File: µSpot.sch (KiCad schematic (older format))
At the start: 35 parts, among them J1 Conn_01x03, SW1 Rotary_Encoder_Switch, U1 AP65211A, U2 MIC5365-3.3YD5, U3 ATtiny406-S, U4 OLED_Display_9616

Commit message: Layout finish
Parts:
- removed C10, C11, C7, C8: 1u, Capacitor_SMD:C_1206_3216Metric_Pad1.42x1.75mm_HandSolder, symbol Device:C_Small
- removed R10: 390k, Resistor_SMD:R_1206_3216Metric_Pad1.42x1.75mm_HandSolder, symbol Device:R_Small
- removed U1: AP65211A, Package_TO_SOT_SMD:TSOT-23-6_HandSoldering, symbol microSpot:AP65211A
- removed U3: ATtiny406-S, Package_SO:SOIC-20W_7.5x12.8mm_P1.27mm, symbol MCU_Microchip_ATtiny:ATtiny406-S
- removed U4: OLED_Display_9616, µSpot:OLED_Display_9616, symbol microSpot:OLED_Display_9616
- added D1: Red, LED_SMD:LED_0805_2012Metric_Pad1.15x1.40mm_HandSolder, symbol Device:LED
- added D2: 2SS100L-W, Diode_SMD:D_SOD-123F, symbol Device:D_Schottky_Small
- added J2: Conn_01x04, Connector_PinSocket_2.54mm:PinSocket_1x04_P2.54mm_Vertical_SMD_Pin1Left, symbol Connector_Generic:Conn_01x04
- added Q7: Q_PMOS_DGS, Package_TO_SOT_SMD:SOT-23, symbol Device:Q_PMOS_DGS
- added R10: 10k, Resistor_SMD:R_0805_2012Metric_Pad1.15x1.40mm_HandSolder, symbol Device:R
- added U1: AP65111AWU, Package_TO_SOT_SMD:TSOT-23-6, symbol Regulator_Switching:AP65111AWU
- added U3: ATtiny404-SS, Package_SO:SOIC-14_3.9x8.7mm_P1.27mm, symbol MCU_Microchip_ATtiny:ATtiny404-SS
- added U5: ADS7029, Package_SO:VSSOP-8_2.3x2mm_P0.5mm, symbol Analog_ADC:ADS7029
- C1, C5: footprint Capacitor_SMD:C_1206_3216Metric_Pad1.42x1.75mm_HandSolder -> Capacitor_SMD:C_0805_2012Metric_Pad1.18x1.45mm_HandSolder
- C2, C3, C4, C6: footprint Capacitor_SMD:C_1206_3216Metric_Pad1.42x1.75mm_HandSolder -> Capacitor_SMD:C_0805_2012Metric_Pad1.15x1.40mm_HandSolder
- C9: value 1u -> 3.3u; footprint Capacitor_SMD:C_1206_3216Metric_Pad1.42x1.75mm_HandSolder -> Capacitor_SMD:C_0805_2012Metric_Pad1.15x1.40mm_HandSolder
- D3, D4: footprint LED_SMD:LED_1206_3216Metric_Pad1.42x1.75mm_HandSolder -> LED_SMD:LED_0805_2012Metric_Pad1.15x1.40mm_HandSolder
- L1: footprint Inductor_SMD:L_Taiyo-Yuden_MD-2020 -> Inductor_SMD:L_0805_2012Metric_Pad1.15x1.40mm_HandSolder
- R1, R3: value 4k7 -> 10k; footprint Resistor_SMD:R_1206_3216Metric_Pad1.42x1.75mm_HandSolder -> Resistor_SMD:R_0805_2012Metric_Pad1.15x1.40mm_HandSolder
- R11: value 10k -> 100k; footprint Resistor_SMD:R_1206_3216Metric_Pad1.42x1.75mm_HandSolder -> Resistor_SMD:R_0805_2012Metric_Pad1.20x1.40mm_HandSolder
- R2, R4, R5, R6, R7, R8, R9: footprint Resistor_SMD:R_1206_3216Metric_Pad1.42x1.75mm_HandSolder -> Resistor_SMD:R_0805_2012Metric_Pad1.15x1.40mm_HandSolder
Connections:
- net ON_LED is gone; now on net TRIGGER: R1.1
- net +3V3: now also C9.1, J2.2 (Pin_2), U3.1 (VCC), U5.7 (AVDD); no longer R11.1
- net +5V: now also D2.1 (K), Q7.3 (S); no longer C5.1, J1.3 (Pin_3), L1.2, R4.1
- net +BATT: now also U1.1 (IN)
- net BAT_VOL: now also U3.2 (PA4)
- net CLK: now also U3.6 (PB3)
- net DT: now also U3.7 (PB2)
- net GND: now also C9.2, J1.1 (Pin_1), R11.2, D1.1 (K), J2.1 (Pin_1), U1.2 (GND), U3.14 (GND), U5.8 (GND); no longer J1.2 (Pin_2)
- net SCL: now also R8.2, J2.3 (Pin_3), U3.9 (PB0); no longer R9.2
- net SDA: now also R9.2, J2.4 (Pin_4), U3.8 (PB1); no longer R8.2
- net SWITCH: now also U3.5 (PA7)
- net TEMP: now also U3.3 (PA5)
- net TRIGGER: now also U3.4 (PA6)
- net UDPI: now also J1.2 (Pin_2), U3.10 (~RESET~/PA0); no longer J1.1 (Pin_1)
- net at C4.2, L1.1: now also U1.3 (SW)
- net at R2.2: now also U1.6 (FB)
- net at C4.1: now also U1.4 (BST)
- new net: D1.2 (A), R10.2
- new net +5VA: C5.1, L1.2, Q7.1 (D), R10.1, R4.1
- new net +5VP: D2.2 (A), J1.3 (Pin_3), Q7.2 (G), R11.1
- new net SCLK: U3.13 (PA3), U5.2 (SCLK)
- new net WELD+: U5.6 (AINP)
- new net WELD-: U5.5 (AINM)
- new net WELD_ADC: U3.12 (PA2), U5.3 (SDO)
- new net WELD_CS: U3.11 (PA1), U5.4 (~CS)
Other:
- note added: "ADC\n"
- moved on the sheet: C1, C4, C5, C6, L1, R2, R4, R5, R8, R9

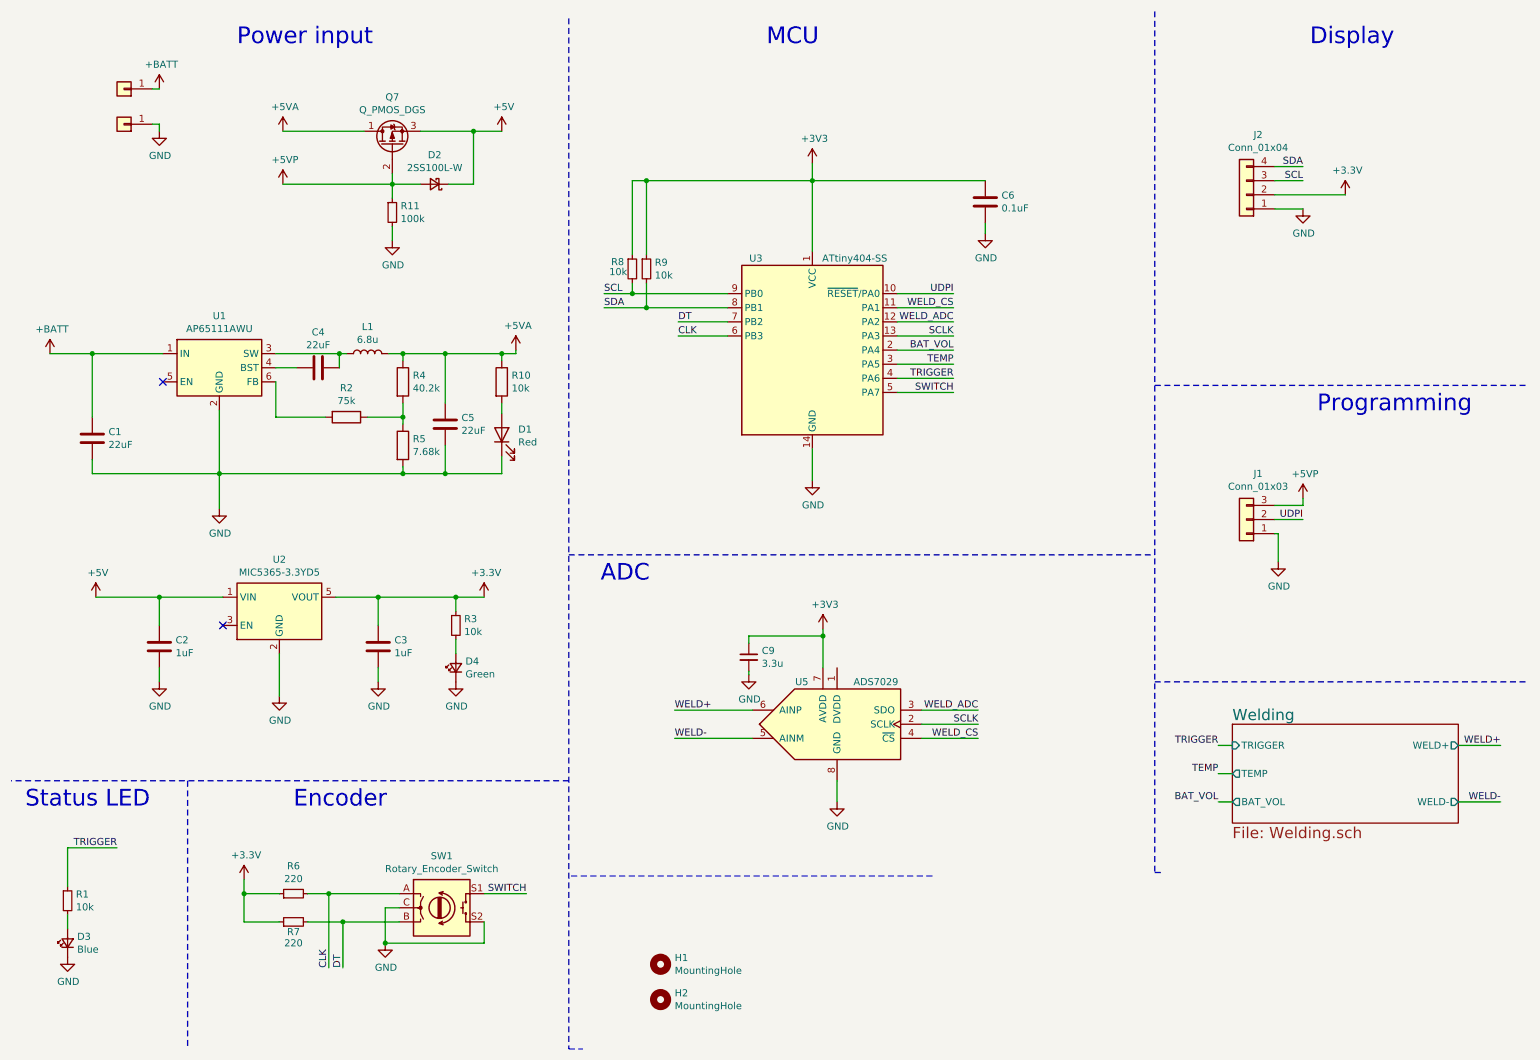
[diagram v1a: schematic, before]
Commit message: Changes FAN3111 footprint and removed 5V
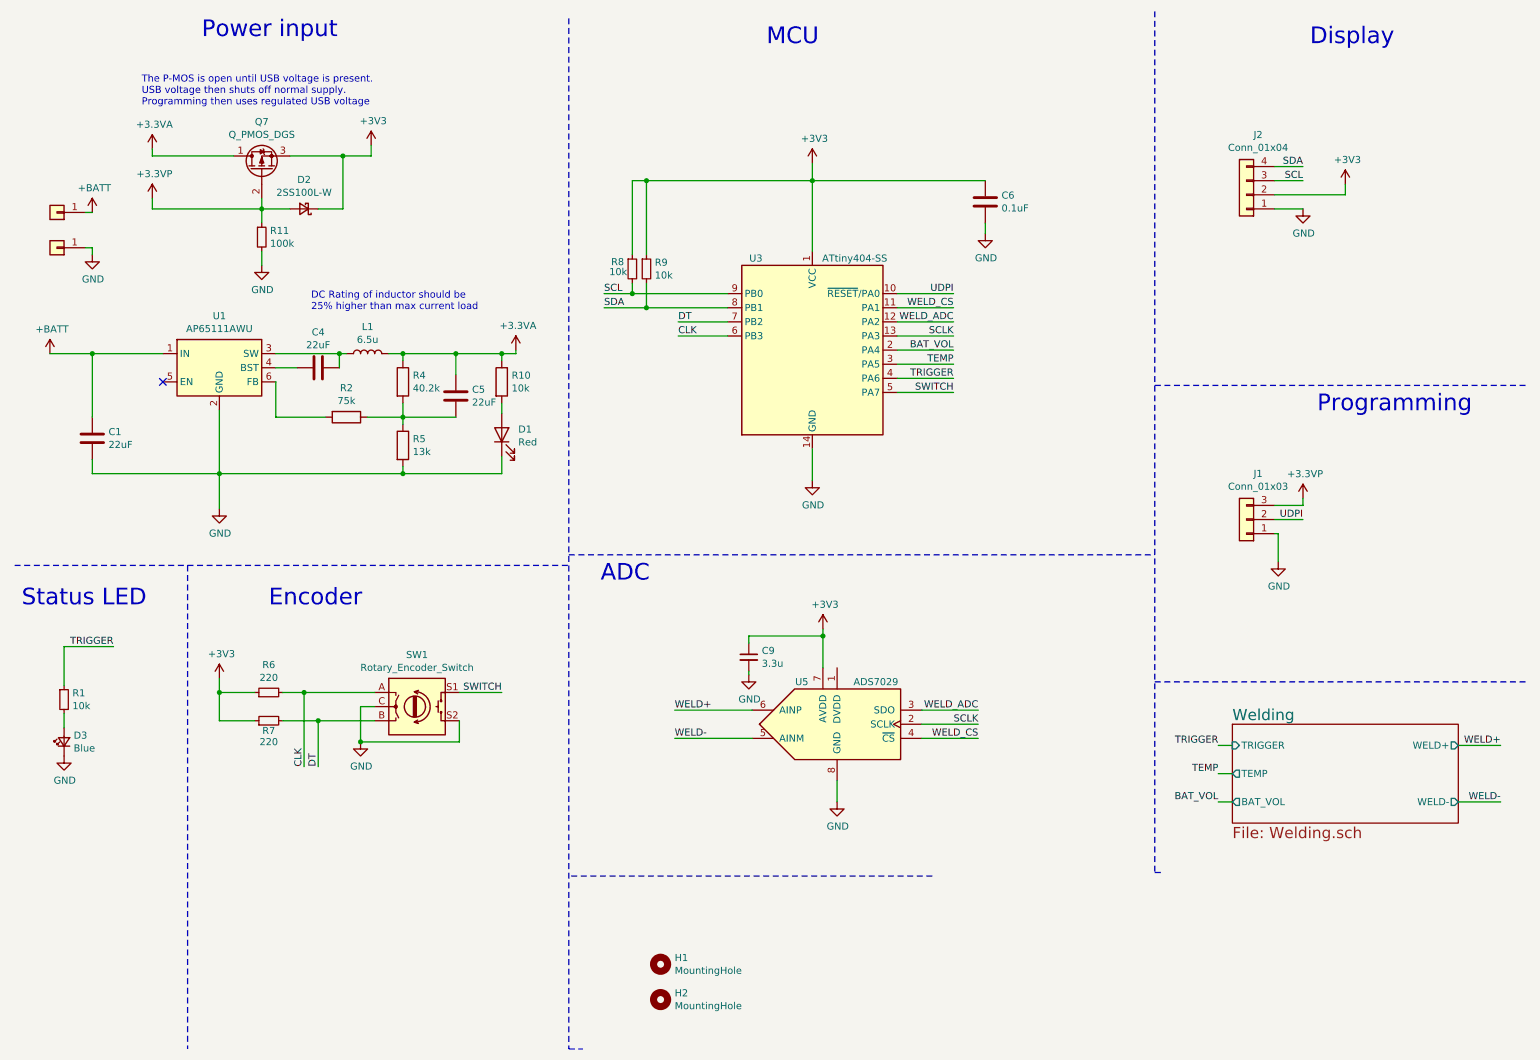
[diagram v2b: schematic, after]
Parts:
- removed C2, C3: 1uF, Capacitor_SMD:C_0805_2012Metric_Pad1.15x1.40mm_HandSolder, symbol Device:C
- removed D4: Green, LED_SMD:LED_0805_2012Metric_Pad1.15x1.40mm_HandSolder, symbol Device:LED_Small
- removed R3: 10k, Resistor_SMD:R_0805_2012Metric_Pad1.15x1.40mm_HandSolder, symbol Device:R_Small
- removed U2: MIC5365-3.3YD5, Package_TO_SOT_SMD:SOT-23-5, symbol Regulator_Linear:MIC5365-3.3YD5
- L1: value 6.8u -> 6.5u
- R5: value 7.68k -> 13k
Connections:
- net +5V is gone; now on net +3V3: D2.1 (K), Q7.3 (S)
- net GND: no longer C5.2
- net at R2.1, R4.2, R5.1: now also C5.2
- net +5VA renamed +3.3VA
- net +5VP renamed +3.3VP
- no-connect marks 2 -> 1
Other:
- note added: "DC Rating of inductor should be \n25% higher than max current load\n"
- note added: "The P-MOS is open until USB voltage is present.\nUSB voltage then shuts off normal supply.\nProgramming then uses regulated USB voltage\n"
- moved on the sheet: C5, D2, D3, Q7, R1, R11, R6, R7, SW1
